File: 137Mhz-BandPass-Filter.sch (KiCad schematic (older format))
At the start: 15 parts, among them J1 SMA, J2 SMA

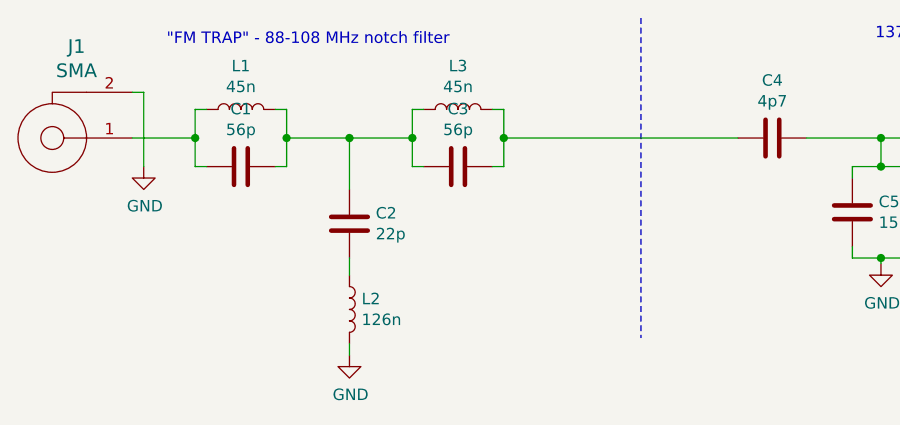
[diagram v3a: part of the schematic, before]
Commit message: Notch filter removed, better inductors position
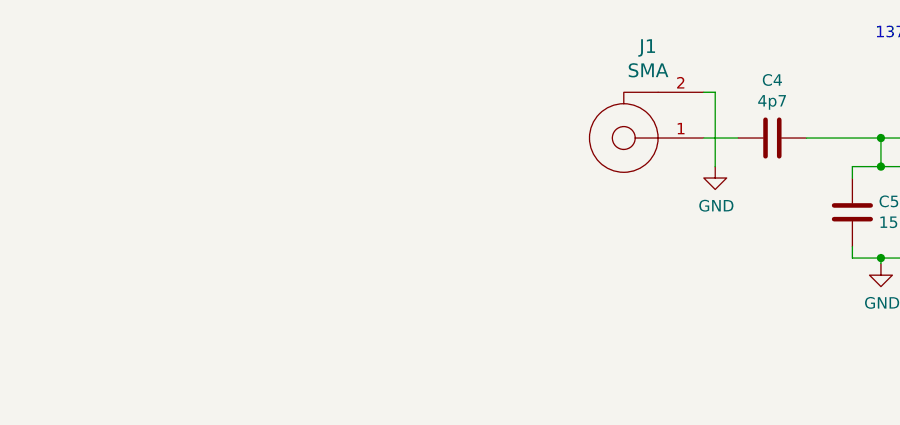
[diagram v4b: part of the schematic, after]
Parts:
- removed C1, C3: 56p, Capacitor_SMD:C_0603_1608Metric_Pad0.99x1.00mm_HandSolder, symbol device:C
- removed C2: 22p, Capacitor_SMD:C_0603_1608Metric_Pad0.99x1.00mm_HandSolder, symbol device:C
- removed L1, L3: 45n, Inductor_SMD:L_Neosid_Air-Coil_SML_2turn_HDM0231A, symbol device:L
- removed L2: 126n, Inductor_SMD:L_Neosid_Air-Coil_SML_5turn_HDM0531A, symbol device:L
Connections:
- net at C4.2: now also J1.1
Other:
- note removed: ""FM TRAP" - 88-108 MHz notch filter"
- moved on the sheet: J1
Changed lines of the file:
@@
 137 Mhz band pass filter
-$Comp
-L device:L L1
-U 1 1 5C988FFB
-P 3800 3375
-F 0 "L1" V 3990 3375 50  0000 C CNN
-F 1 "45n" V 3899 3375 50  0000 C CNN
-F 2 "Inductor_SMD:L_Neosid_Air-Coil_SML_2turn_HDM0231A" H 3800 3375 50  0001 C CNN
-F 3 "" H 3800 3375 50  0001 C CNN
-	1    3800 3375
-	0    -1   -1   0
-$EndComp
-$Comp
-L device:C C1
-U 1 1 5C989001
-P 3800 3625
-F 0 "C1" V 3548 3625 50  0000 C CNN
-F 1 "56p" V 3639 3625 50  0000 C CNN
-F 2 "Capacitor_SMD:C_0603_1608Metric_Pad0.99x1.00mm_HandSolder" H 3838 3475 50  0001 C CNN
-F 3 "" H 3800 3625 50  0001 C CNN
-	1    3800 3625
-	0    1    1    0
-$EndComp
-Wire Wire Line
-	3950 3625 4000 3625
-Wire Wire Line
-	4000 3625 4000 3500
-Wire Wire Line
-	4000 3375 3950 3375
-Connection ~ 4000 3500
-Wire Wire Line
-	4000 3500 4000 3375
-Wire Wire Line
-	3650 3625 3600 3625
-Wire Wire Line
-	3600 3625 3600 3500
-Wire Wire Line
-	3600 3375 3650 3375
-Connection ~ 3600 3500
-Wire Wire Line
-	3600 3500 3600 3375
-$Comp
-L device:C C2
-U 1 1 5C98A175
-P 4275 3875
-F 0 "C2" H 4160 3829 50  0000 R CNN
-F 1 "22p" H 4160 3920 50  0000 R CNN
-F 2 "Capacitor_SMD:C_0603_1608Metric_Pad0.99x1.00mm_HandSolder" H 4313 3725 50  0001 C CNN
-F 3 "" H 4275 3875 50  0001 C CNN
-	1    4275 3875
-	-1   0    0    1
-$EndComp
-$Comp
-L device:L L2
-U 1 1 5C98A1C3
-P 4275 4250
-F 0 "L2" H 4328 4296 50  0000 L CNN
-F 1 "126n" H 4328 4205 50  0000 L CNN
-F 2 "Inductor_SMD:L_Neosid_Air-Coil_SML_5turn_HDM0531A" H 4275 4250 50  0001 C CNN
-F 3 "" H 4275 4250 50  0001 C CNN
-	1    4275 4250
-	1    0    0    -1
-$EndComp
-$Comp
-L power:GND #PWR0103
-U 1 1 5C98A221
-P 4275 4450
-F 0 "#PWR0103" H 4275 4200 50  0001 C CNN
-F 1 "GND" H 4280 4277 50  0000 C CNN
-F 2 "" H 4275 4450 50  0001 C CNN
-F 3 "" H 4275 4450 50  0001 C CNN
-	1    4275 4450
-	1    0    0    -1
-$EndComp
-$Comp
-L device:L L3
-U 1 1 5C98A2C3
-P 4750 3375
-F 0 "L3" V 4940 3375 50  0000 C CNN
-F 1 "45n" V 4849 3375 50  0000 C CNN
-F 2 "Inductor_SMD:L_Neosid_Air-Coil_SML_2turn_HDM0231A" H 4750 3375 50  0001 C CNN
-F 3 "" H 4750 3375 50  0001 C CNN
-	1    4750 3375
-	0    -1   -1   0
-$EndComp
-$Comp
-L device:C C3
-U 1 1 5C98A2C9
-P 4750 3625
-F 0 "C3" V 4498 3625 50  0000 C CNN
-F 1 "56p" V 4589 3625 50  0000 C CNN
-F 2 "Capacitor_SMD:C_0603_1608Metric_Pad0.99x1.00mm_HandSolder" H 4788 3475 50  0001 C CNN
-F 3 "" H 4750 3625 50  0001 C CNN
-	1    4750 3625
-	0    1    1    0
-$EndComp
-Wire Wire Line
-	4900 3625 4950 3625
-Wire Wire Line
-	4950 3625 4950 3500
-Wire Wire Line
-	4950 3375 4900 3375
-Connection ~ 4950 3500
-Wire Wire Line
-	4950 3500 4950 3375
-Wire Wire Line
-	4600 3625 4550 3625
-Wire Wire Line
-	4550 3625 4550 3500
-Wire Wire Line
-	4550 3375 4600 3375
-Connection ~ 4550 3500
-Wire Wire Line
-	4550 3500 4550 3375
-Wire Wire Line
-	4000 3500 4275 3500
-Wire Wire Line
-	4275 3725 4275 3500
-Connection ~ 4275 3500
-Wire Wire Line
-	4275 3500 4550 3500
-Wire Wire Line
-	4275 4025 4275 4100
-Wire Wire Line
-	4275 4400 4275 4450
-Wire Wire Line
-	4950 3500 5975 3500
-Text Notes 3475 3100 0    50   ~ 0
-"FM TRAP" - 88-108 MHz notch filter
-Wire Notes Line
-	5550 2975 5550 4375
 $Comp
 L MLAB_CONNECTORS:SMA J1
 U 1 1 5C9A2C08
-P 2975 3500
-F 0 "J1" H 2869 3100 60  0000 C CNN
-F 1 "SMA" H 2869 3206 60  0000 C CNN
-F 2 "Connector_Coaxial:SMA_Molex_73251-1153_EdgeMount_Horizontal" H 2975 3500 60  0001 C CNN
-F 3 "" H 2975 3500 60  0000 C CNN
-	1    2975 3500
+P 5475 3500
+F 0 "J1" H 5369 3100 60  0000 C CNN
+F 1 "SMA" H 5369 3206 60  0000 C CNN
+F 2 "Connector_Coaxial:SMA_Molex_73251-1153_EdgeMount_Horizontal" H 5475 3500 60  0001 C CNN
+F 3 "" H 5475 3500 60  0000 C CNN
+	1    5475 3500
 	-1   0    0    1
 $EndComp
@@
 Wire Wire Line
 	8225 3700 8225 3750
-Wire Wire Line
-	3325 3500 3600 3500
 $Comp
 L power:GND #PWR0105
 U 1 1 5C9A5252
-P 3375 3625
-F 0 "#PWR0105" H 3375 3375 50  0001 C CNN
-F 1 "GND" H 3380 3452 50  0000 C CNN
-F 2 "" H 3375 3625 50  0001 C CNN
-F 3 "" H 3375 3625 50  0001 C CNN
-	1    3375 3625
+P 5875 3625
+F 0 "#PWR0105" H 5875 3375 50  0001 C CNN
+F 1 "GND" H 5880 3452 50  0000 C CNN
+F 2 "" H 5875 3625 50  0001 C CNN
+F 3 "" H 5875 3625 50  0001 C CNN
+	1    5875 3625
 	1    0    0    -1
 $EndComp
 Wire Wire Line
-	3325 3300 3375 3300
+	5825 3300 5875 3300
 Wire Wire Line
-	3375 3300 3375 3625
+	5875 3300 5875 3625
+Wire Wire Line
+	5975 3500 5825 3500
 $EndSCHEMATC

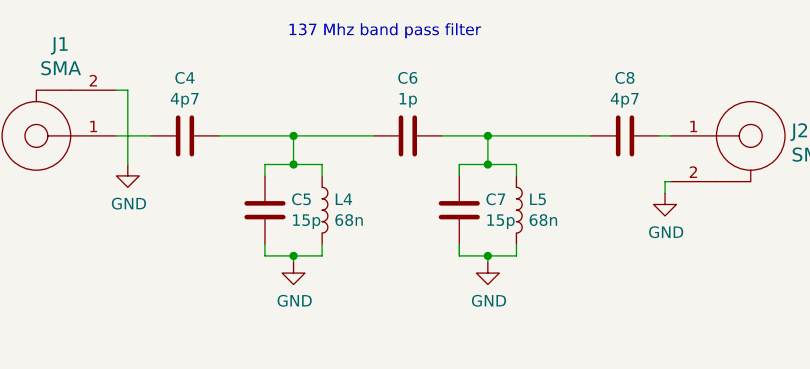
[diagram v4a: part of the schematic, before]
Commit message: Coils type change, new layout, anotation reset
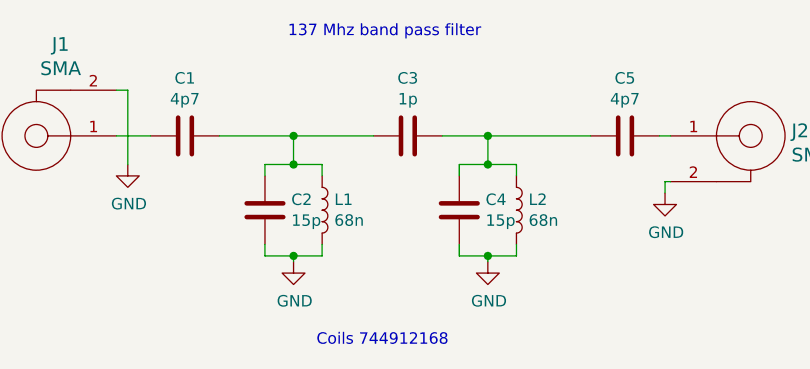
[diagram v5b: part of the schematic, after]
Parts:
- L1: renamed from L4; footprint kicad-footprints-master:1515SQ-68N -> kicad-footprints-master:Wurth-WE-CAIR-AirCoil-4,83x3,81
- L2: renamed from L5; footprint kicad-footprints-master:1515SQ-68N -> kicad-footprints-master:Wurth-WE-CAIR-AirCoil-4,83x3,81
- renumbered C4 to C1, C5 to C2, C6 to C3, C7 to C4, C8 to C5
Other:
- note added: "Coils 744912168"
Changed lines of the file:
@@
 $EndDescr
 $Comp
-L device:C C4
+L device:C C1
 U 1 1 5C988072
 P 6125 3500
-F 0 "C4" V 5873 3500 50  0000 C CNN
+F 0 "C1" V 5873 3500 50  0000 C CNN
 F 1 "4p7" V 5964 3500 50  0000 C CNN
 F 2 "Capacitor_SMD:C_0603_1608Metric_Pad0.99x1.00mm_HandSolder" H 6163 3350 50  0001 C CNN
@@
 $EndComp
 $Comp
-L device:L L4
+L device:L L1
 U 1 1 5C9880A3
 P 6725 3825
-F 0 "L4" H 6778 3871 50  0000 L CNN
+F 0 "L1" H 6778 3871 50  0000 L CNN
 F 1 "68n" H 6778 3780 50  0000 L CNN
-F 2 "kicad-footprints-master:1515SQ-68N" H 6725 3825 50  0001 C CNN
+F 2 "kicad-footprints-master:Wurth-WE-CAIR-AirCoil-4,83x3,81" H 6725 3825 50  0001 C CNN
 F 3 "" H 6725 3825 50  0001 C CNN
 	1    6725 3825
@@
 $EndComp
 $Comp
-L device:C C6
+L device:C C3
 U 1 1 5C988184
 P 7100 3500
-F 0 "C6" V 6848 3500 50  0000 C CNN
+F 0 "C3" V 6848 3500 50  0000 C CNN
 F 1 "1p" V 6939 3500 50  0000 C CNN
 F 2 "Capacitor_SMD:C_0603_1608Metric_Pad0.99x1.00mm_HandSolder" H 7138 3350 50  0001 C CNN
@@
 $EndComp
 $Comp
-L device:C C8
+L device:C C5
 U 1 1 5C9881D4
 P 8050 3500
-F 0 "C8" V 7798 3500 50  0000 C CNN
+F 0 "C5" V 7798 3500 50  0000 C CNN
 F 1 "4p7" V 7889 3500 50  0000 C CNN
 F 2 "Capacitor_SMD:C_0603_1608Metric_Pad0.99x1.00mm_HandSolder" H 8088 3350 50  0001 C CNN
@@
 $EndComp
 $Comp
-L device:C C5
+L device:C C2
 U 1 1 5C988200
 P 6475 3825
-F 0 "C5" H 6360 3779 50  0000 R CNN
+F 0 "C2" H 6360 3779 50  0000 R CNN
 F 1 "15p" H 6360 3870 50  0000 R CNN
 F 2 "Capacitor_SMD:C_0603_1608Metric_Pad0.99x1.00mm_HandSolder" H 6513 3675 50  0001 C CNN
@@
 $EndComp
 $Comp
-L power:GND #PWR0101
+L power:GND #PWR02
 U 1 1 5C9883DD
 P 6600 4050
-F 0 "#PWR0101" H 6600 3800 50  0001 C CNN
+F 0 "#PWR02" H 6600 3800 50  0001 C CNN
 F 1 "GND" H 6605 3877 50  0000 C CNN
 F 2 "" H 6600 4050 50  0001 C CNN
@@
 Connection ~ 6600 3500
 $Comp
-L device:L L5
+L device:L L2
 U 1 1 5C988781
 P 7575 3825
-F 0 "L5" H 7628 3871 50  0000 L CNN
+F 0 "L2" H 7628 3871 50  0000 L CNN
 F 1 "68n" H 7628 3780 50  0000 L CNN
-F 2 "kicad-footprints-master:1515SQ-68N" H 7575 3825 50  0001 C CNN
+F 2 "kicad-footprints-master:Wurth-WE-CAIR-AirCoil-4,83x3,81" H 7575 3825 50  0001 C CNN
 F 3 "" H 7575 3825 50  0001 C CNN
 	1    7575 3825
@@
 $EndComp
 $Comp
-L device:C C7
+L device:C C4
 U 1 1 5C988787
 P 7325 3825
-F 0 "C7" H 7210 3779 50  0000 R CNN
+F 0 "C4" H 7210 3779 50  0000 R CNN
 F 1 "15p" H 7210 3870 50  0000 R CNN
 F 2 "Capacitor_SMD:C_0603_1608Metric_Pad0.99x1.00mm_HandSolder" H 7363 3675 50  0001 C CNN
@@
 $EndComp
 $Comp
-L power:GND #PWR0102
+L power:GND #PWR03
 U 1 1 5C98878D
 P 7450 4050
-F 0 "#PWR0102" H 7450 3800 50  0001 C CNN
+F 0 "#PWR03" H 7450 3800 50  0001 C CNN
 F 1 "GND" H 7455 3877 50  0000 C CNN
 F 2 "" H 7450 4050 50  0001 C CNN
@@
 	8200 3500 8250 3500
 $Comp
-L power:GND #PWR0104
+L power:GND #PWR04
 U 1 1 5C9A39B3
 P 8225 3750
-F 0 "#PWR0104" H 8225 3500 50  0001 C CNN
+F 0 "#PWR04" H 8225 3500 50  0001 C CNN
 F 1 "GND" H 8230 3577 50  0000 C CNN
 F 2 "" H 8225 3750 50  0001 C CNN
@@
 	8225 3700 8225 3750
 $Comp
-L power:GND #PWR0105
+L power:GND #PWR01
 U 1 1 5C9A5252
 P 5875 3625
-F 0 "#PWR0105" H 5875 3375 50  0001 C CNN
+F 0 "#PWR01" H 5875 3375 50  0001 C CNN
 F 1 "GND" H 5880 3452 50  0000 C CNN
 F 2 "" H 5875 3625 50  0001 C CNN
@@
 Wire Wire Line
 	5975 3500 5825 3500
+Text Notes 6700 4425 0    50   ~ 0
+Coils 744912168
 $EndSCHEMATC

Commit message: Final v0.1
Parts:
- removed J1, J2: SMA, Connector_Coaxial:SMA_Molex_73251-1153_EdgeMount_Horizontal, symbol MLAB_CONNECTORS:SMA
- added J1, J3: Conn_01x01, Connector_Wire:SolderWirePad_1x01_SMD_5x10mm, symbol Connector:Conn_01x01
- added MK1, MK2, MK3, MK4: Mounting_Hole_PAD, MountingHole:MountingHole_3.2mm_M3_Pad, symbol Mechanical:Mounting_Hole_PAD
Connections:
- net GND: now also MK1.1, MK2.1, MK3.1, MK4.1
- net at C1.2: now also J1.1 (Pin_1)
- net at C5.1: now also J3.1 (Pin_1)
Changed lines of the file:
@@
 Text Notes 6575 3075 0    50   ~ 0
 137 Mhz band pass filter
-$Comp
-L MLAB_CONNECTORS:SMA J1
-U 1 1 5C9A2C08
-P 5475 3500
-F 0 "J1" H 5369 3100 60  0000 C CNN
-F 1 "SMA" H 5369 3206 60  0000 C CNN
-F 2 "Connector_Coaxial:SMA_Molex_73251-1153_EdgeMount_Horizontal" H 5475 3500 60  0001 C CNN
-F 3 "" H 5475 3500 60  0000 C CNN
-	1    5475 3500
-	-1   0    0    1
-$EndComp
-$Comp
-L MLAB_CONNECTORS:SMA J2
-U 1 1 5C9A2DC6
-P 8600 3500
-F 0 "J2" H 8778 3522 60  0000 L CNN
-F 1 "SMA" H 8778 3416 60  0000 L CNN
-F 2 "Connector_Coaxial:SMA_Molex_73251-1153_EdgeMount_Horizontal" H 8600 3500 60  0001 C CNN
-F 3 "" H 8600 3500 60  0000 C CNN
-	1    8600 3500
-	1    0    0    -1
-$EndComp
 Wire Wire Line
 	8200 3500 8250 3500
-$Comp
-L power:GND #PWR04
-U 1 1 5C9A39B3
-P 8225 3750
-F 0 "#PWR04" H 8225 3500 50  0001 C CNN
-F 1 "GND" H 8230 3577 50  0000 C CNN
-F 2 "" H 8225 3750 50  0001 C CNN
-F 3 "" H 8225 3750 50  0001 C CNN
-	1    8225 3750
-	1    0    0    -1
-$EndComp
-Wire Wire Line
-	8250 3700 8225 3700
-Wire Wire Line
-	8225 3700 8225 3750
-$Comp
-L power:GND #PWR01
-U 1 1 5C9A5252
-P 5875 3625
-F 0 "#PWR01" H 5875 3375 50  0001 C CNN
-F 1 "GND" H 5880 3452 50  0000 C CNN
-F 2 "" H 5875 3625 50  0001 C CNN
-F 3 "" H 5875 3625 50  0001 C CNN
-	1    5875 3625
-	1    0    0    -1
-$EndComp
-Wire Wire Line
-	5825 3300 5875 3300
-Wire Wire Line
-	5875 3300 5875 3625
 Wire Wire Line
 	5975 3500 5825 3500
 Text Notes 6700 4425 0    50   ~ 0
 Coils 744912168
+$Comp
+L Mechanical:Mounting_Hole_PAD MK1
+U 1 1 5CA77022
+P 9725 4350
+F 0 "MK1" V 9962 4355 50  0000 C CNN
+F 1 "Mounting_Hole_PAD" V 9871 4355 50  0000 C CNN
+F 2 "MountingHole:MountingHole_3.2mm_M3_Pad" H 9725 4350 50  0001 C CNN
+F 3 "" H 9725 4350 50  0001 C CNN
+	1    9725 4350
+	0    -1   -1   0
+$EndComp
+$Comp
+L power:GND #PWR0101
+U 1 1 5CA77133
+P 9875 4400
+F 0 "#PWR0101" H 9875 4150 50  0001 C CNN
+F 1 "GND" H 9880 4227 50  0000 C CNN
+F 2 "" H 9875 4400 50  0001 C CNN
+F 3 "" H 9875 4400 50  0001 C CNN
+	1    9875 4400
+	1    0    0    -1
+$EndComp
+Wire Wire Line
+	9825 4350 9875 4350
+Wire Wire Line
+	9875 4350 9875 4400
+$Comp
+L Mechanical:Mounting_Hole_PAD MK2
+U 1 1 5CA775FC
+P 9725 4675
+F 0 "MK2" V 9962 4680 50  0000 C CNN
+F 1 "Mounting_Hole_PAD" V 9871 4680 50  0000 C CNN
+F 2 "MountingHole:MountingHole_3.2mm_M3_Pad" H 9725 4675 50  0001 C CNN
+F 3 "" H 9725 4675 50  0001 C CNN
+	1    9725 4675
+	0    -1   -1   0
+$EndComp
+$Comp
+L power:GND #PWR0102
+U 1 1 5CA77602
+P 9875 4725
+F 0 "#PWR0102" H 9875 4475 50  0001 C CNN
+F 1 "GND" H 9880 4552 50  0000 C CNN
+F 2 "" H 9875 4725 50  0001 C CNN
+F 3 "" H 9875 4725 50  0001 C CNN
+	1    9875 4725
+	1    0    0    -1
+$EndComp
+Wire Wire Line
+	9825 4675 9875 4675
+Wire Wire Line
+	9875 4675 9875 4725
+$Comp
+L Mechanical:Mounting_Hole_PAD MK3
+U 1 1 5CA77A8A
+P 9725 4975
+F 0 "MK3" V 9962 4980 50  0000 C CNN
+F 1 "Mounting_Hole_PAD" V 9871 4980 50  0000 C CNN
+F 2 "MountingHole:MountingHole_3.2mm_M3_Pad" H 9725 4975 50  0001 C CNN
+F 3 "" H 9725 4975 50  0001 C CNN
+	1    9725 4975
+	0    -1   -1   0
+$EndComp
+$Comp
+L power:GND #PWR0103
+U 1 1 5CA77A90
+P 9875 5025
+F 0 "#PWR0103" H 9875 4775 50  0001 C CNN
+F 1 "GND" H 9880 4852 50  0000 C CNN
+F 2 "" H 9875 5025 50  0001 C CNN
+F 3 "" H 9875 5025 50  0001 C CNN
+	1    9875 5025
+	1    0    0    -1
+$EndComp
+Wire Wire Line
+	9825 4975 9875 4975
+Wire Wire Line
+	9875 4975 9875 5025
+$Comp
+L Mechanical:Mounting_Hole_PAD MK4
+U 1 1 5CA77A98
+P 9725 5300
+F 0 "MK4" V 9962 5305 50  0000 C CNN
+F 1 "Mounting_Hole_PAD" V 9871 5305 50  0000 C CNN
+F 2 "MountingHole:MountingHole_3.2mm_M3_Pad" H 9725 5300 50  0001 C CNN
+F 3 "" H 9725 5300 50  0001 C CNN
+	1    9725 5300
+	0    -1   -1   0
+$EndComp
+$Comp
+L power:GND #PWR0104
+U 1 1 5CA77A9E
+P 9875 5350
+F 0 "#PWR0104" H 9875 5100 50  0001 C CNN
+F 1 "GND" H 9880 5177 50  0000 C CNN
+F 2 "" H 9875 5350 50  0001 C CNN
+F 3 "" H 9875 5350 50  0001 C CNN
+	1    9875 5350
+	1    0    0    -1
+$EndComp
+Wire Wire Line
+	9825 5300 9875 5300
+Wire Wire Line
+	9875 5300 9875 5350
+$Comp
+L Connector:Conn_01x01 J3
+U 1 1 5CA7811E
+P 8450 3500
+F 0 "J3" H 8530 3542 50  0000 L CNN
+F 1 "Conn_01x01" H 8530 3451 50  0000 L CNN
+F 2 "Connector_Wire:SolderWirePad_1x01_SMD_5x10mm" H 8450 3500 50  0001 C CNN
+F 3 "~" H 8450 3500 50  0001 C CNN
+	1    8450 3500
+	1    0    0    -1
+$EndComp
+$Comp
+L Connector:Conn_01x01 J1
+U 1 1 5CA7878B
+P 5625 3500
+F 0 "J1" H 5545 3275 50  0000 C CNN
+F 1 "Conn_01x01" H 5545 3366 50  0000 C CNN
+F 2 "Connector_Wire:SolderWirePad_1x01_SMD_5x10mm" H 5625 3500 50  0001 C CNN
+F 3 "~" H 5625 3500 50  0001 C CNN
+	1    5625 3500
+	-1   0    0    1
+$EndComp
 $EndSCHEMATC

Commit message: Added pads for shielding between coils
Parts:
- added J2, J4: Conn_01x01, Measurement_Points:Measurement_Point_Square-SMD-Pad_Big, symbol 137Mhz-BandPass-Filter-rescue:Conn_01x01-Connector
- C1, C2, C3, C4, C5: symbol device:C -> 137Mhz-BandPass-Filter-rescue:C-device
- J1, J3: value Conn_01x01 -> SMA; symbol Connector:Conn_01x01 -> 137Mhz-BandPass-Filter-rescue:Conn_01x01-Connector
- L1, L2: symbol device:L -> 137Mhz-BandPass-Filter-rescue:L-device
- MK1, MK2, MK3, MK4: symbol Mechanical:Mounting_Hole_PAD -> 137Mhz-BandPass-Filter-rescue:Mounting_Hole_PAD-Mechanical
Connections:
- net GND: now also J2.1 (Pin_1), J4.1 (Pin_1)
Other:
- moved on the sheet: C1, C2, C3, C4, C5, J1, J3, L1, L2
